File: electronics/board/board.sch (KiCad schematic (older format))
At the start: 58 parts, among them J1 Conn_02x05_Odd_Even, J2 USB_A, J3 Micro_SD_Card_Det_Hirose_DM3AT, SW1 SW_Push, U1 JW5211, U2 JW5211, U3 JW5211, U4 F1C100s, U5 SST26VF080A-104I/SN, U6 USBLC6-2SC6, Y1 Crystal_GND24

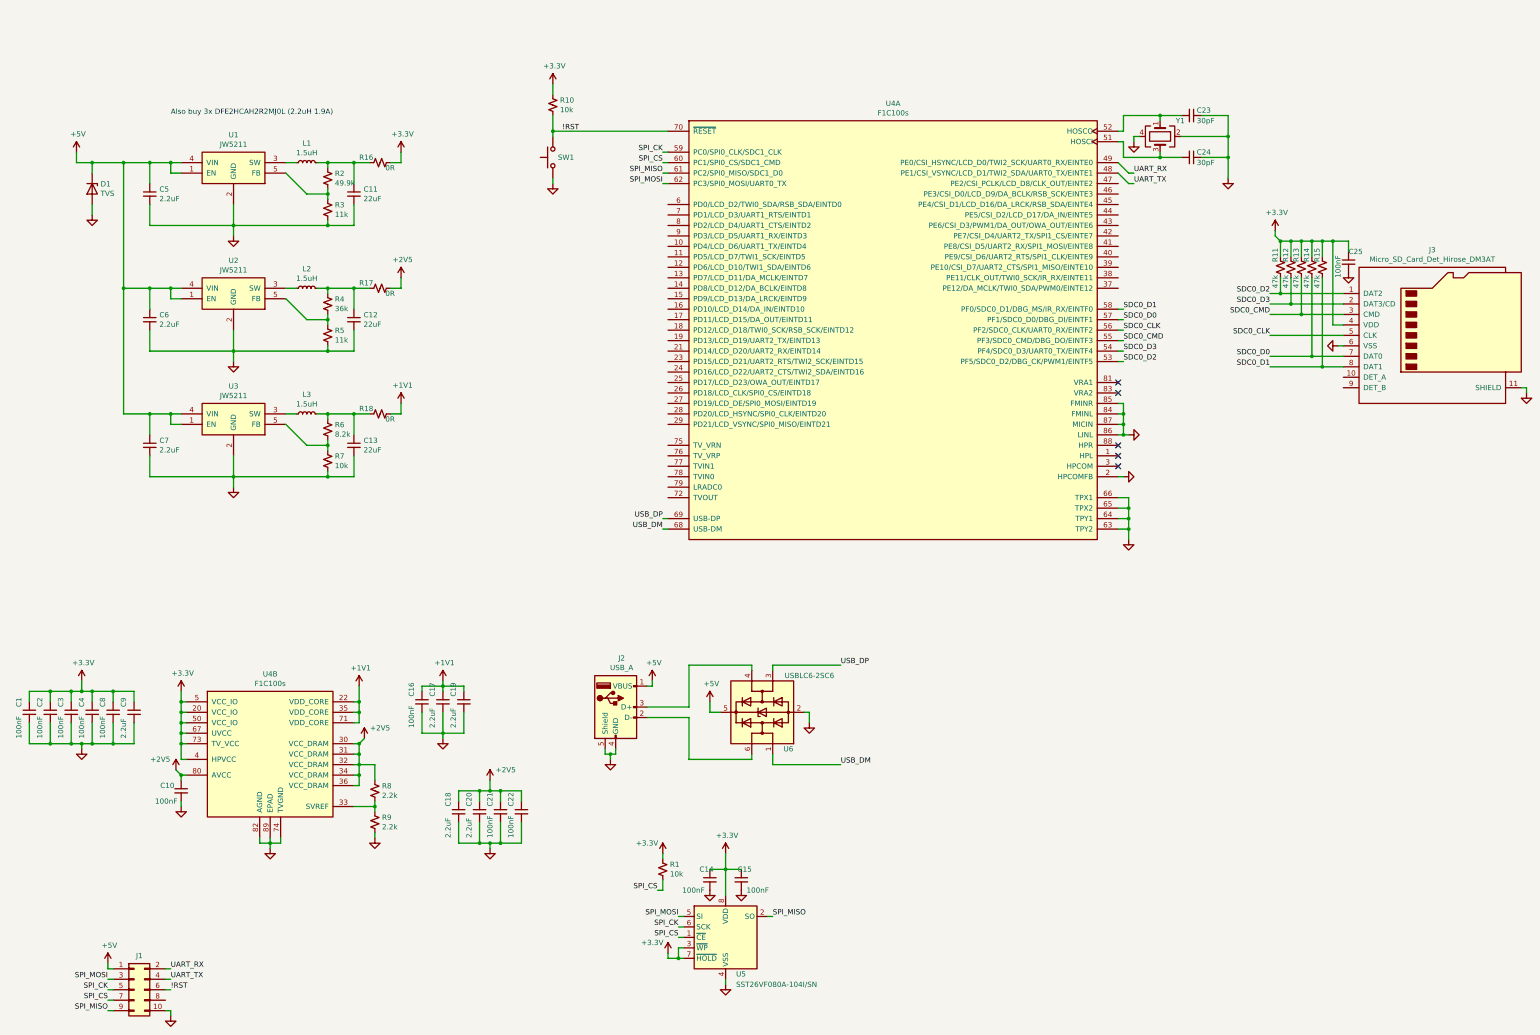
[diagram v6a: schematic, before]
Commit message: Added ATECC608B security chip and filled in the rest of footprints.
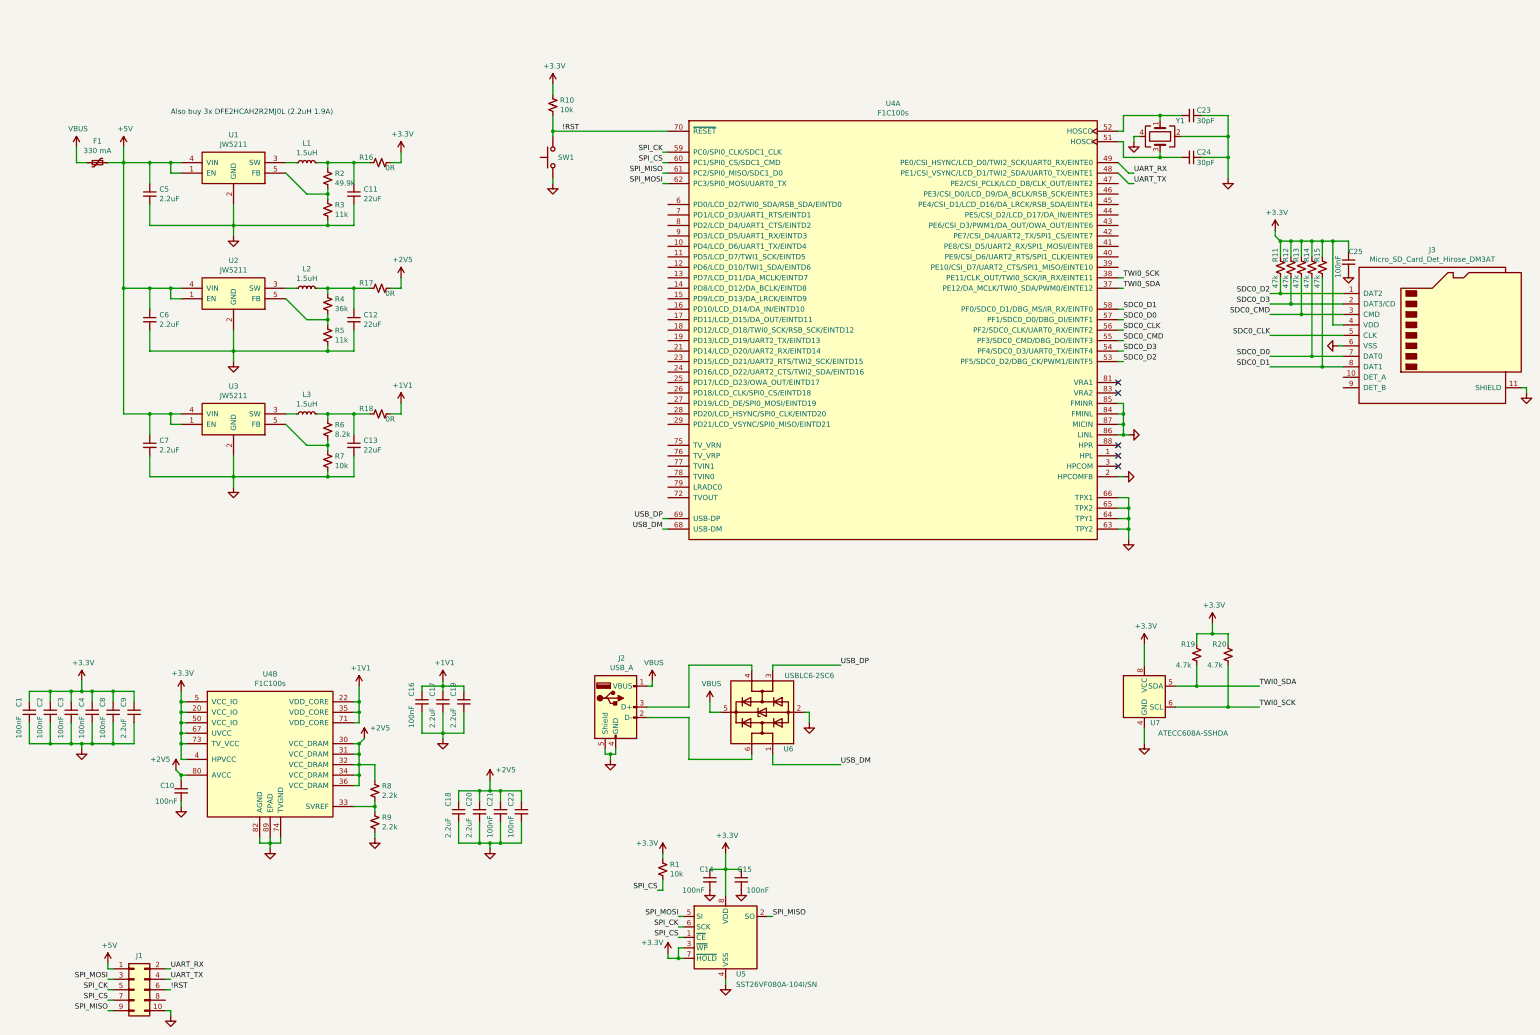
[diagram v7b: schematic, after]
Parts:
- removed D1: TVS, symbol Device:D_Zener
- added F1: 330 mA, Fuse:Fuse_0603_1608Metric, symbol Device:Polyfuse_Small
- added R19, R20: 4.7k, Resistor_SMD:R_0603_1608Metric, symbol Device:R_Small_US
- added U7: ATECC608A-SSHDA, Package_SO:SOIC-8_3.9x4.9mm_P1.27mm, symbol Security:ATECC608A-SSHDA
- J1: footprint (none) -> Connector_PinSocket_2.54mm:PinSocket_2x05_P2.54mm_Vertical
- J2: footprint (none) -> Connector_USB:USB_A_CNCTech_1001-011-01101_Horizontal; MPN (none) -> 1001-011-01101
- R1, R10, R11, R12, R13, R14, R15, R16, R17, R18, R2, R3, R4, R5, R6, R7, R8, R9: footprint (none) -> Resistor_SMD:R_0603_1608Metric
- SW1: footprint (none) -> Button_Switch_SMD:SW_SPST_TL3342
- Y1: footprint (none) -> Crystal:Crystal_SMD_Abracon_ABM8G-4Pin_3.2x2.5mm; MPN (none) -> ABM8G-24.000MHZ-18-D2Y-T
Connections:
- net +3V3: now also R19.1, R20.1, U7.8 (VCC)
- net +5V: now also F1.1; no longer J2.1 (VBUS), U6.5 (VBUS)
- net GND: now also U7.4 (GND)
- net TWI0_SDA: now reaches U4.37 (PE12/DA_MCLK/TWI0_SDA/PWM0/EINTE12)
- net TWI0_SDA: now also R19.2, U7.5 (SDA)
- net TWI0_SCK: now reaches U4.38 (PE11/CLK_OUT/TWI0_SCK/IR_RX/EINTE11)
- net TWI0_SCK: now also R20.2, U7.6 (SCL)
- new net VBUS: F1.2, J2.1 (VBUS), U6.5 (VBUS)

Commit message: Arranged the parts.
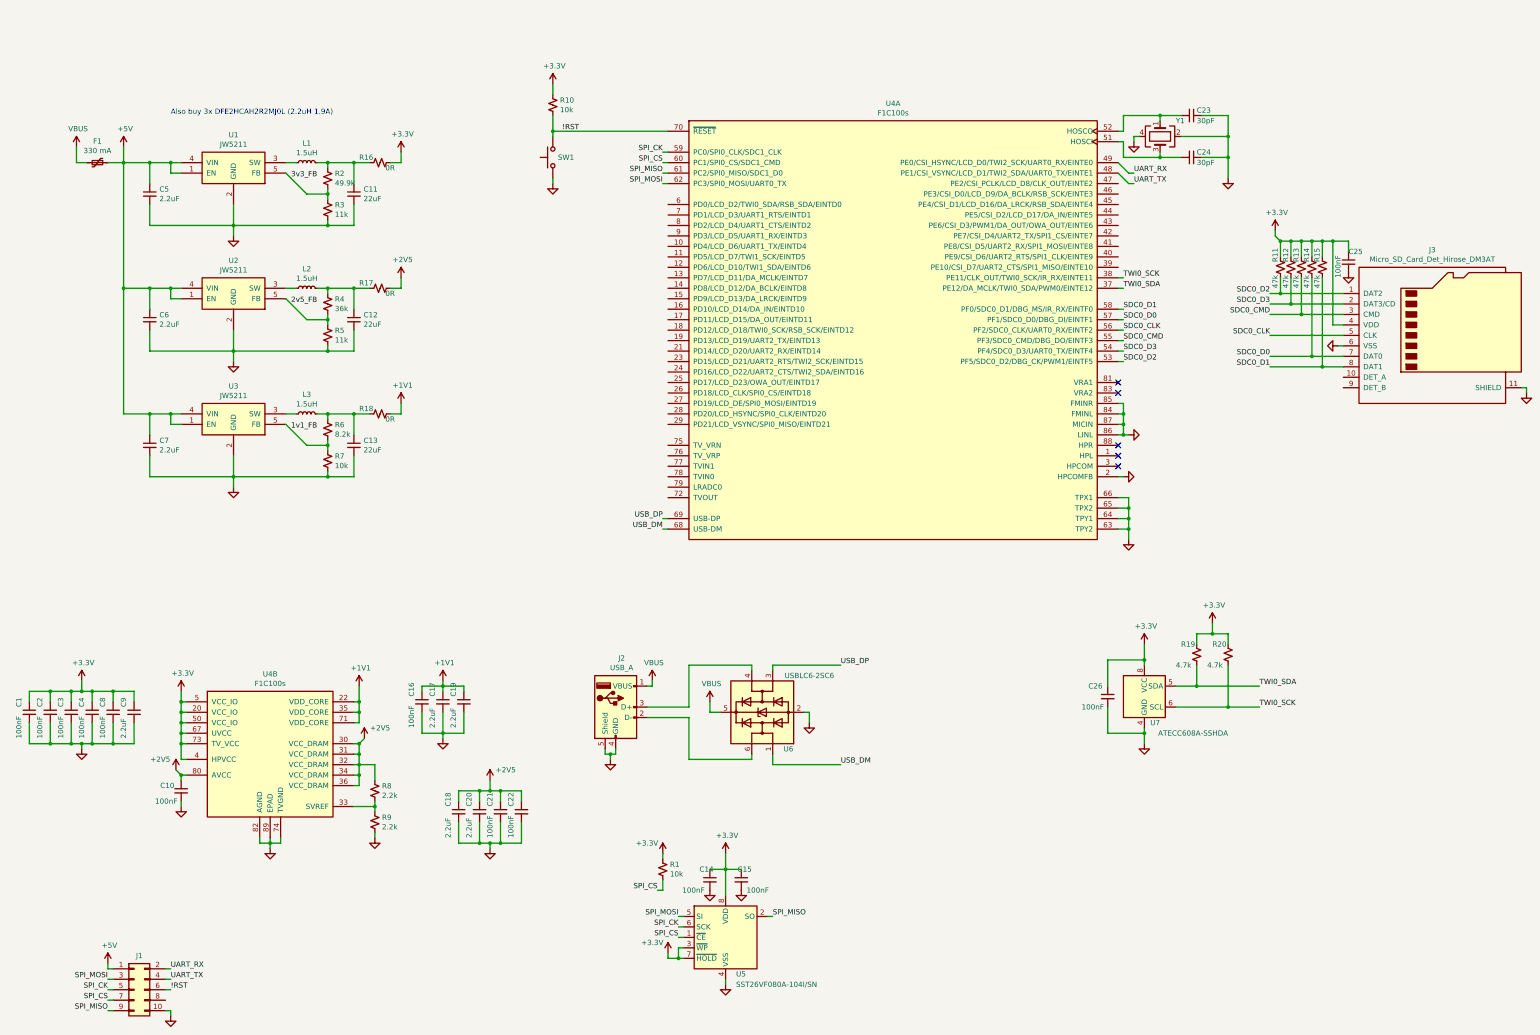
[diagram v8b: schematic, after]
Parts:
- added C26: 100nF, Capacitor_SMD:C_0603_1608Metric, symbol Device:C_Small
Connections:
- net +3V3: now also C26.1
- net GND: now also C26.2
- net 3v3_FB: now reaches R2.2, R3.1, U1.5 (FB)
- net 2v5_FB: now reaches R4.2, R5.1, U2.5 (FB)
- net 1v1_FB: now reaches R6.2, R7.1, U3.5 (FB)
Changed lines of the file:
@@
 $EndComp
 Wire Wire Line
-	11450 7600 11450 7450
+	11450 7600 11450 7500
 Wire Wire Line
-	11450 6850 11450 6650
+	11450 6850 11450 6800
 Wire Wire Line
 	11200 3150 11250 3150
@@
 Wire Wire Line
 	11950 6550 12100 6550
+$Comp
+L Device:C_Small C26
+U 1 1 61A28D52
+P 11100 7150
+F 0 "C26" H 11050 7250 50  0000 R CNN
+F 1 "100nF" H 10850 7050 50  0000 L CNN
+F 2 "Capacitor_SMD:C_0603_1608Metric" H 11100 7150 50  0001 C CNN
+F 3 "~" H 11100 7150 50  0001 C CNN
+	1    11100 7150
+	1    0    0    -1
+$EndComp
+Wire Wire Line
+	11100 7050 11100 6800
+Wire Wire Line
+	11100 6800 11450 6800
+Connection ~ 11450 6800
+Wire Wire Line
+	11450 6800 11450 6650
+Wire Wire Line
+	11100 7250 11100 7500
+Wire Wire Line
+	11100 7500 11450 7500
+Connection ~ 11450 7500
+Wire Wire Line
+	11450 7500 11450 7450
+Text Label 3300 2200 0    50   ~ 0
+3v3_FB
+Text Label 3300 3400 0    50   ~ 0
+2v5_FB
+Text Label 3300 4600 0    50   ~ 0
+1v1_FB
 $EndSCHEMATC
